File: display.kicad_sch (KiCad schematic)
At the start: 9 parts

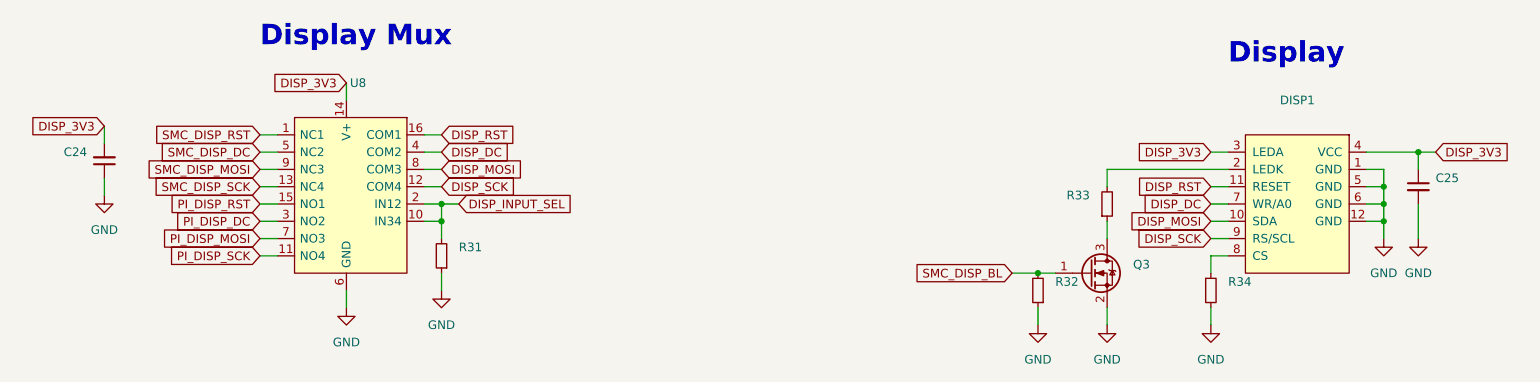
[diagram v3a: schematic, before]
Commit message: layout: update footprint for TP4056M
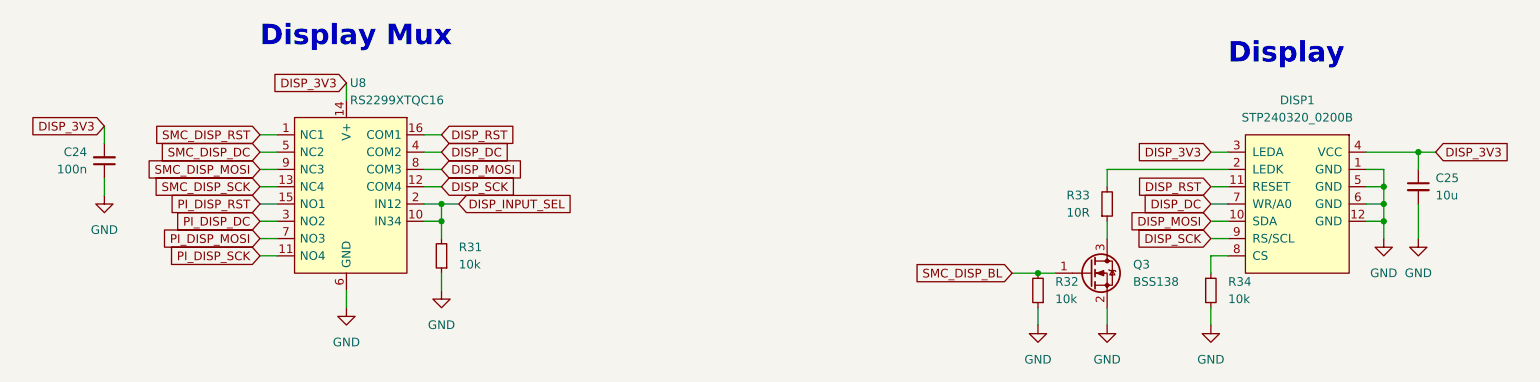
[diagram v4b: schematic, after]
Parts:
- C24: value (none) -> 100n; footprint (none) -> Capacitor_SMD:C_0402_1005Metric
- C25: value (none) -> 10u; footprint (none) -> Capacitor_SMD:C_0402_1005Metric
- DISP1: value (none) -> STP240320_0200B; footprint (none) -> Connector_Molex:Molex_SlimStack_54722-0164_2x08_P0.50mm_Vertical
- Q3: value (none) -> BSS138; footprint (none) -> Package_TO_SOT_SMD:SOT-23
- R31, R32, R34: value (none) -> 10k; footprint (none) -> Resistor_SMD:R_0402_1005Metric
- R33: value (none) -> 10R; footprint (none) -> Resistor_SMD:R_0402_1005Metric
- U8: value (none) -> RS2299XTQC16; footprint (none) -> Package_DFN_QFN:QFN-16-1EP_3x3mm_P0.5mm_EP1.7x1.7mm
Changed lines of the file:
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@@
       (effects (font (size 1.27 1.27)) (justify right))
     )
-    (property "Value" "" (id 1) (at 80.5306 96.52 0)
-      (effects (font (size 1.27 1.27)) (justify right))
-    )
-    (property "Footprint" "" (id 2) (at 97.79 88.9 0)
+    (property "Value" "RS2299XTQC16" (id 1) (at 80.5306 96.52 0)
+      (effects (font (size 1.27 1.27)) (justify right))
+    )
+    (property "Footprint" "Package_DFN_QFN:QFN-16-1EP_3x3mm_P0.5mm_EP1.7x1.7mm" (id 2) (at 97.79 88.9 0)
       (effects (font (size 1.27 1.27)) (justify left) hide)
     )
@@
       (effects (font (size 1.27 1.27)) (justify right))
     )
-    (property "Value" "" (id 1) (at 189.23 113.0299 0)
-      (effects (font (size 1.27 1.27)) (justify right))
-    )
-    (property "Footprint" "" (id 2) (at 191.77 111.76 0)
+    (property "Value" "10R" (id 1) (at 189.23 113.0299 0)
+      (effects (font (size 1.27 1.27)) (justify right))
+    )
+    (property "Footprint" "Resistor_SMD:R_0402_1005Metric" (id 2) (at 191.77 111.76 0)
       (effects (font (size 1.27 1.27)) hide)
     )
@@
       (effects (font (size 1.27 1.27)) (justify right))
     )
-    (property "Value" "" (id 1) (at 96.52 120.6499 0)
-      (effects (font (size 1.27 1.27)) (justify right))
-    )
-    (property "Footprint" "" (id 2) (at 93.98 119.38 0)
+    (property "Value" "10k" (id 1) (at 96.52 120.6499 0)
+      (effects (font (size 1.27 1.27)) (justify right))
+    )
+    (property "Footprint" "Resistor_SMD:R_0402_1005Metric" (id 2) (at 93.98 119.38 0)
       (effects (font (size 1.27 1.27)) hide)
     )
@@
     (in_bom yes) (on_board yes) (fields_autoplaced)
     (property "Reference" "DISP1" (id 0) (at 219.71 96.52 0))
-    (property "Value" "" (id 1) (at 219.71 99.06 0))
-    (property "Footprint" "" (id 2) (at 219.71 101.6 0)
+    (property "Value" "STP240320_0200B" (id 1) (at 219.71 99.06 0))
+    (property "Footprint" "Connector_Molex:Molex_SlimStack_54722-0164_2x08_P0.50mm_Vertical" (id 2) (at 219.71 101.6 0)
       (effects (font (size 1.27 1.27)) hide)
     )
@@
       (effects (font (size 1.27 1.27)) (justify right))
     )
-    (property "Value" "" (id 1) (at 184.15 125.7299 0)
-      (effects (font (size 1.27 1.27)) (justify right))
-    )
-    (property "Footprint" "" (id 2) (at 181.61 124.46 0)
+    (property "Value" "10k" (id 1) (at 184.15 125.7299 0)
+      (effects (font (size 1.27 1.27)) (justify right))
+    )
+    (property "Footprint" "Resistor_SMD:R_0402_1005Metric" (id 2) (at 181.61 124.46 0)
       (effects (font (size 1.27 1.27)) hide)
     )
@@
       (effects (font (size 1.27 1.27)) (justify left))
     )
-    (property "Value" "" (id 1) (at 209.55 125.7299 0)
-      (effects (font (size 1.27 1.27)) (justify left))
-    )
-    (property "Footprint" "" (id 2) (at 207.01 124.46 0)
+    (property "Value" "10k" (id 1) (at 209.55 125.7299 0)
+      (effects (font (size 1.27 1.27)) (justify left))
+    )
+    (property "Footprint" "Resistor_SMD:R_0402_1005Metric" (id 2) (at 207.01 124.46 0)
       (effects (font (size 1.27 1.27)) hide)
     )
@@
       (effects (font (size 1.27 1.27)) (justify left))
     )
-    (property "Value" "" (id 1) (at 240.03 110.4962 0)
-      (effects (font (size 1.27 1.27)) (justify left))
-    )
-    (property "Footprint" "" (id 2) (at 237.49 109.22 0)
+    (property "Value" "10u" (id 1) (at 240.03 110.4962 0)
+      (effects (font (size 1.27 1.27)) (justify left))
+    )
+    (property "Footprint" "Capacitor_SMD:C_0402_1005Metric" (id 2) (at 237.49 109.22 0)
       (effects (font (size 1.27 1.27)) hide)
     )
@@
       (effects (font (size 1.27 1.27)) (justify right))
     )
-    (property "Value" "" (id 1) (at 41.91 106.6735 0)
-      (effects (font (size 1.27 1.27)) (justify right))
-    )
-    (property "Footprint" "" (id 2) (at 44.45 105.41 0)
+    (property "Value" "100n" (id 1) (at 41.91 106.6735 0)
+      (effects (font (size 1.27 1.27)) (justify right))
+    )
+    (property "Footprint" "Capacitor_SMD:C_0402_1005Metric" (id 2) (at 44.45 105.41 0)
       (effects (font (size 1.27 1.27)) hide)
     )
@@
       (effects (font (size 1.27 1.27)) (justify left))
     )
-    (property "Value" "" (id 1) (at 195.58 123.1899 0)
-      (effects (font (size 1.27 1.27)) (justify left))
-    )
-    (property "Footprint" "" (id 2) (at 194.31 123.825 0)
+    (property "Value" "BSS138" (id 1) (at 195.58 123.1899 0)
+      (effects (font (size 1.27 1.27)) (justify left))
+    )
+    (property "Footprint" "Package_TO_SOT_SMD:SOT-23" (id 2) (at 194.31 123.825 0)
       (effects (font (size 1.27 1.27) italic) (justify left) hide)
     )

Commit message: routing: begin routing
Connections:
- net DISP_DC: now also U8.16 (COM1); no longer U8.4 (COM2)
- net DISP_MOSI: now also U8.4 (COM2); no longer U8.8 (COM3)
- net DISP_RST: now also U8.8 (COM3); no longer U8.16 (COM1)
- net PI_DISP_DC: now also U8.15 (NO1); no longer U8.3 (NO2)
- net PI_DISP_MOSI: now also U8.3 (NO2); no longer U8.7 (NO3)
- net PI_DISP_RST: now also U8.7 (NO3); no longer U8.15 (NO1)
- net SMC_DISP_DC: now also U8.1 (NC1); no longer U8.5 (NC2)
- net SMC_DISP_MOSI: now also U8.5 (NC2); no longer U8.9 (NC3)
- net SMC_DISP_RST: now also U8.9 (NC3); no longer U8.1 (NC1)
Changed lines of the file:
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@@
     )
   )
-  (global_label "SMC_DISP_RST" (shape input) (at 67.31 101.6 180) (fields_autoplaced)
+  (global_label "SMC_DISP_RST" (shape input) (at 67.31 106.68 180) (fields_autoplaced)
     (effects (font (size 1.27 1.27)) (justify right))
-    (property "Intersheet References" "${INTERSHEET_REFS}" (id 0) (at 51.2293 101.5206 0)
+    (property "Intersheet References" "${INTERSHEET_REFS}" (id 0) (at 51.2293 106.6006 0)
       (effects (font (size 1.27 1.27)) (justify right) hide)
     )
@@
     )
   )
-  (global_label "PI_DISP_MOSI" (shape input) (at 67.31 116.84 180) (fields_autoplaced)
+  (global_label "PI_DISP_MOSI" (shape input) (at 67.31 114.3 180) (fields_autoplaced)
     (effects (font (size 1.27 1.27)) (justify right))
-    (property "Intersheet References" "${INTERSHEET_REFS}" (id 0) (at 52.1364 116.7606 0)
+    (property "Intersheet References" "${INTERSHEET_REFS}" (id 0) (at 52.1364 114.2206 0)
       (effects (font (size 1.27 1.27)) (justify right) hide)
     )
   )
-  (global_label "DISP_MOSI" (shape input) (at 93.98 106.68 0) (fields_autoplaced)
+  (global_label "DISP_MOSI" (shape input) (at 93.98 104.14 0) (fields_autoplaced)
     (effects (font (size 1.27 1.27)) (justify left))
-    (property "Intersheet References" "${INTERSHEET_REFS}" (id 0) (at 106.3112 106.6006 0)
+    (property "Intersheet References" "${INTERSHEET_REFS}" (id 0) (at 106.3112 104.0606 0)
       (effects (font (size 1.27 1.27)) (justify left) hide)
     )
   )
-  (global_label "DISP_RST" (shape input) (at 93.98 101.6 0) (fields_autoplaced)
+  (global_label "DISP_RST" (shape input) (at 93.98 106.68 0) (fields_autoplaced)
     (effects (font (size 1.27 1.27)) (justify left))
-    (property "Intersheet References" "${INTERSHEET_REFS}" (id 0) (at 105.1621 101.5206 0)
+    (property "Intersheet References" "${INTERSHEET_REFS}" (id 0) (at 105.1621 106.6006 0)
       (effects (font (size 1.27 1.27)) (justify left) hide)
     )
@@
     )
   )
-  (global_label "SMC_DISP_MOSI" (shape input) (at 67.31 106.68 180) (fields_autoplaced)
+  (global_label "SMC_DISP_MOSI" (shape input) (at 67.31 104.14 180) (fields_autoplaced)
     (effects (font (size 1.27 1.27)) (justify right))
-    (property "Intersheet References" "${INTERSHEET_REFS}" (id 0) (at 50.0802 106.7594 0)
+    (property "Intersheet References" "${INTERSHEET_REFS}" (id 0) (at 50.0802 104.2194 0)
       (effects (font (size 1.27 1.27)) (justify right) hide)
     )
@@
     )
   )
-  (global_label "PI_DISP_RST" (shape input) (at 67.31 111.76 180) (fields_autoplaced)
+  (global_label "PI_DISP_RST" (shape input) (at 67.31 116.84 180) (fields_autoplaced)
     (effects (font (size 1.27 1.27)) (justify right))
-    (property "Intersheet References" "${INTERSHEET_REFS}" (id 0) (at 53.2855 111.6806 0)
+    (property "Intersheet References" "${INTERSHEET_REFS}" (id 0) (at 53.2855 116.7606 0)
       (effects (font (size 1.27 1.27)) (justify right) hide)
     )
@@
     )
   )
-  (global_label "DISP_DC" (shape input) (at 93.98 104.14 0) (fields_autoplaced)
+  (global_label "DISP_DC" (shape input) (at 93.98 101.6 0) (fields_autoplaced)
     (effects (font (size 1.27 1.27)) (justify left))
-    (property "Intersheet References" "${INTERSHEET_REFS}" (id 0) (at 104.255 104.0606 0)
+    (property "Intersheet References" "${INTERSHEET_REFS}" (id 0) (at 104.255 101.5206 0)
       (effects (font (size 1.27 1.27)) (justify left) hide)
     )
   )
-  (global_label "SMC_DISP_DC" (shape input) (at 67.31 104.14 180) (fields_autoplaced)
+  (global_label "SMC_DISP_DC" (shape input) (at 67.31 101.6 180) (fields_autoplaced)
     (effects (font (size 1.27 1.27)) (justify right))
-    (property "Intersheet References" "${INTERSHEET_REFS}" (id 0) (at 52.1364 104.0606 0)
+    (property "Intersheet References" "${INTERSHEET_REFS}" (id 0) (at 52.1364 101.5206 0)
       (effects (font (size 1.27 1.27)) (justify right) hide)
     )
@@
     )
   )
-  (global_label "PI_DISP_DC" (shape input) (at 67.31 114.3 180) (fields_autoplaced)
+  (global_label "PI_DISP_DC" (shape input) (at 67.31 111.76 180) (fields_autoplaced)
     (effects (font (size 1.27 1.27)) (justify right))
-    (property "Intersheet References" "${INTERSHEET_REFS}" (id 0) (at 54.1926 114.2206 0)
+    (property "Intersheet References" "${INTERSHEET_REFS}" (id 0) (at 54.1926 111.6806 0)
       (effects (font (size 1.27 1.27)) (justify right) hide)
     )

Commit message: layout, routing: relayout and reroute board
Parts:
- C24: value 100n -> (none); footprint Capacitor_SMD:C_0402_1005Metric -> (none)
- C25: value 10u -> (none); footprint Capacitor_SMD:C_0402_1005Metric -> (none)
- DISP1: value STP240320_0200B -> (none); footprint Connector_Molex:Molex_SlimStack_54722-0164_2x08_P0.50mm_Vertical -> (none)
- Q3: value BSS138 -> (none); footprint Package_TO_SOT_SMD:SOT-23 -> (none)
- R31, R32, R34: value 10k -> (none); footprint Resistor_SMD:R_0402_1005Metric -> (none)
- R33: value 10R -> (none); footprint Resistor_SMD:R_0402_1005Metric -> (none)
- U8: value RS2299XTQC16 -> (none); footprint Package_DFN_QFN:QFN-16-1EP_3x3mm_P0.5mm_EP1.7x1.7mm -> (none)
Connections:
- net DISP_BL_MOS_D: now reaches Q3.3 (D), R33.1
- net DISP_LEDK: now reaches DISP1.2 (LEDK), R33.2
- net DISP_CS: now reaches DISP1.8 (CS), R34.1
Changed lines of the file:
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@@
     (effects (font (size 3 3) (thickness 0.6) bold) (justify left bottom))
   )
+  (label "DISP_BL_MOS_D" (at 191.77 115.57 180)
+    (effects (font (size 0.8 0.8)) (justify right bottom))
+  )
+  (label "DISP_CS" (at 208.28 119.38 180)
+    (effects (font (size 0.8 0.8)) (justify right bottom))
+  )
+  (label "DISP_LEDK" (at 195.58 106.68 180)
+    (effects (font (size 1.27 1.27)) (justify right bottom))
+  )
   (global_label "DISP_MOSI" (shape input) (at 207.01 114.3 180) (fields_autoplaced)
     (effects (font (size 1.27 1.27)) (justify right))
@@
       (effects (font (size 1.27 1.27)) (justify right))
     )
-    (property "Value" "RS2299XTQC16" (id 1) (at 80.5306 96.52 0)
-      (effects (font (size 1.27 1.27)) (justify right))
-    )
-    (property "Footprint" "Package_DFN_QFN:QFN-16-1EP_3x3mm_P0.5mm_EP1.7x1.7mm" (id 2) (at 97.79 88.9 0)
+    (property "Value" "" (id 1) (at 80.5306 96.52 0)
+      (effects (font (size 1.27 1.27)) (justify right))
+    )
+    (property "Footprint" "" (id 2) (at 97.79 88.9 0)
       (effects (font (size 1.27 1.27)) (justify left) hide)
     )
@@
       (effects (font (size 1.27 1.27)) (justify right))
     )
-    (property "Value" "10R" (id 1) (at 189.23 113.0299 0)
-      (effects (font (size 1.27 1.27)) (justify right))
-    )
-    (property "Footprint" "Resistor_SMD:R_0402_1005Metric" (id 2) (at 191.77 111.76 0)
+    (property "Value" "" (id 1) (at 189.23 113.0299 0)
+      (effects (font (size 1.27 1.27)) (justify right))
+    )
+    (property "Footprint" "" (id 2) (at 191.77 111.76 0)
       (effects (font (size 1.27 1.27)) hide)
     )
@@
       (effects (font (size 1.27 1.27)) (justify right))
     )
-    (property "Value" "10k" (id 1) (at 96.52 120.6499 0)
-      (effects (font (size 1.27 1.27)) (justify right))
-    )
-    (property "Footprint" "Resistor_SMD:R_0402_1005Metric" (id 2) (at 93.98 119.38 0)
+    (property "Value" "" (id 1) (at 96.52 120.6499 0)
+      (effects (font (size 1.27 1.27)) (justify right))
+    )
+    (property "Footprint" "" (id 2) (at 93.98 119.38 0)
       (effects (font (size 1.27 1.27)) hide)
     )
@@
     (in_bom yes) (on_board yes) (fields_autoplaced)
     (property "Reference" "DISP1" (id 0) (at 219.71 96.52 0))
-    (property "Value" "STP240320_0200B" (id 1) (at 219.71 99.06 0))
-    (property "Footprint" "Connector_Molex:Molex_SlimStack_54722-0164_2x08_P0.50mm_Vertical" (id 2) (at 219.71 101.6 0)
+    (property "Value" "" (id 1) (at 219.71 99.06 0))
+    (property "Footprint" "" (id 2) (at 219.71 101.6 0)
       (effects (font (size 1.27 1.27)) hide)
     )
@@
       (effects (font (size 1.27 1.27)) (justify right))
     )
-    (property "Value" "10k" (id 1) (at 184.15 125.7299 0)
-      (effects (font (size 1.27 1.27)) (justify right))
-    )
-    (property "Footprint" "Resistor_SMD:R_0402_1005Metric" (id 2) (at 181.61 124.46 0)
+    (property "Value" "" (id 1) (at 184.15 125.7299 0)
+      (effects (font (size 1.27 1.27)) (justify right))
+    )
+    (property "Footprint" "" (id 2) (at 181.61 124.46 0)
       (effects (font (size 1.27 1.27)) hide)
     )
@@
       (effects (font (size 1.27 1.27)) (justify left))
     )
-    (property "Value" "10k" (id 1) (at 209.55 125.7299 0)
-      (effects (font (size 1.27 1.27)) (justify left))
-    )
-    (property "Footprint" "Resistor_SMD:R_0402_1005Metric" (id 2) (at 207.01 124.46 0)
+    (property "Value" "" (id 1) (at 209.55 125.7299 0)
+      (effects (font (size 1.27 1.27)) (justify left))
+    )
+    (property "Footprint" "" (id 2) (at 207.01 124.46 0)
       (effects (font (size 1.27 1.27)) hide)
     )
@@
       (effects (font (size 1.27 1.27)) (justify left))
     )
-    (property "Value" "10u" (id 1) (at 240.03 110.4962 0)
-      (effects (font (size 1.27 1.27)) (justify left))
-    )
-    (property "Footprint" "Capacitor_SMD:C_0402_1005Metric" (id 2) (at 237.49 109.22 0)
+    (property "Value" "" (id 1) (at 240.03 110.4962 0)
+      (effects (font (size 1.27 1.27)) (justify left))
+    )
+    (property "Footprint" "" (id 2) (at 237.49 109.22 0)
       (effects (font (size 1.27 1.27)) hide)
     )
@@
       (effects (font (size 1.27 1.27)) (justify right))
     )
-    (property "Value" "100n" (id 1) (at 41.91 106.6735 0)
-      (effects (font (size 1.27 1.27)) (justify right))
-    )
-    (property "Footprint" "Capacitor_SMD:C_0402_1005Metric" (id 2) (at 44.45 105.41 0)
+    (property "Value" "" (id 1) (at 41.91 106.6735 0)
+      (effects (font (size 1.27 1.27)) (justify right))
+    )
+    (property "Footprint" "" (id 2) (at 44.45 105.41 0)
       (effects (font (size 1.27 1.27)) hide)
     )
@@
       (effects (font (size 1.27 1.27)) (justify left))
     )
-    (property "Value" "BSS138" (id 1) (at 195.58 123.1899 0)
-      (effects (font (size 1.27 1.27)) (justify left))
-    )
-    (property "Footprint" "Package_TO_SOT_SMD:SOT-23" (id 2) (at 194.31 123.825 0)
+    (property "Value" "" (id 1) (at 195.58 123.1899 0)
+      (effects (font (size 1.27 1.27)) (justify left))
+    )
+    (property "Footprint" "" (id 2) (at 194.31 123.825 0)
       (effects (font (size 1.27 1.27) italic) (justify left) hide)
     )

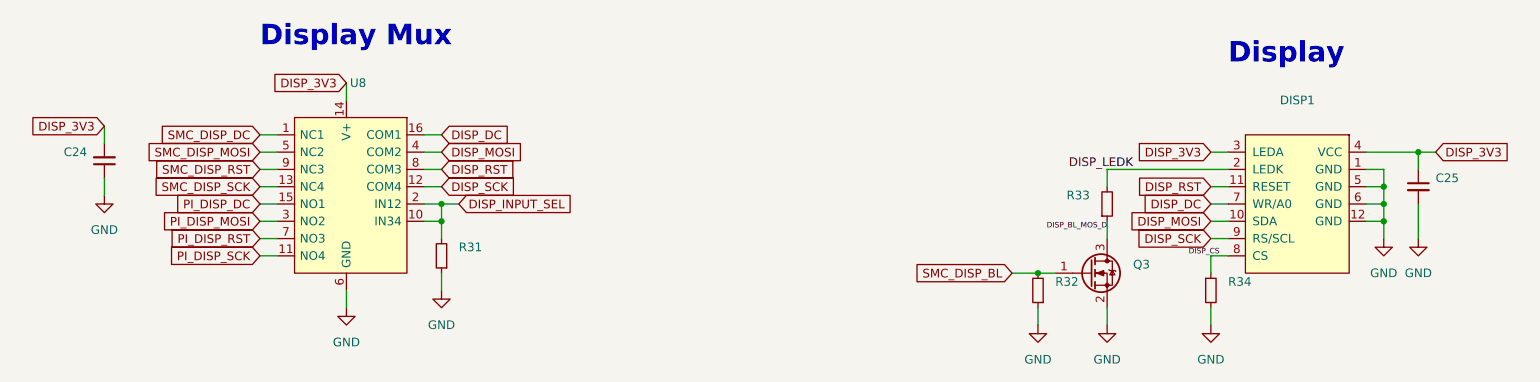
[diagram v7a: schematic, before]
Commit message: layout: add testpoints, extra mounting hole, grounding clips
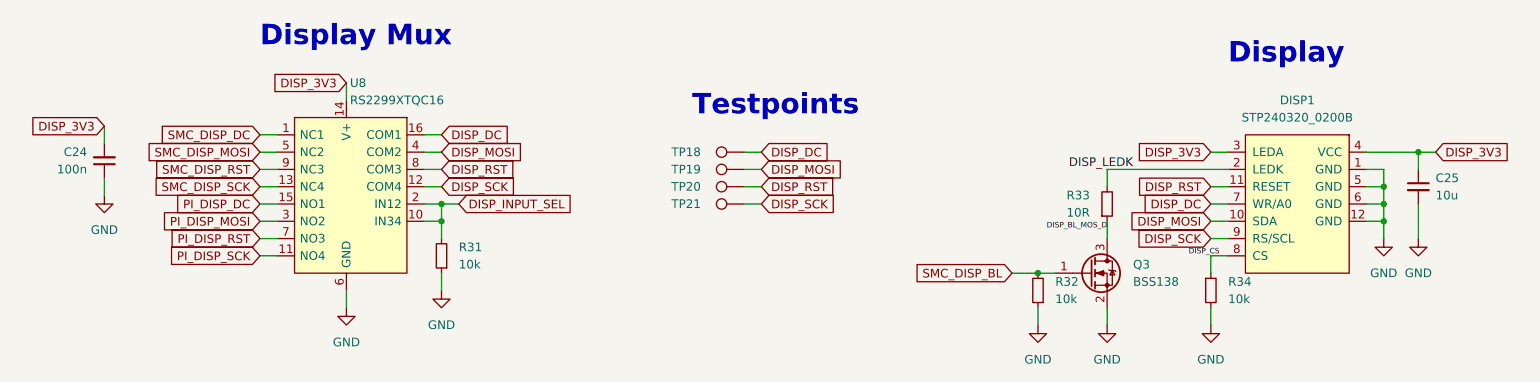
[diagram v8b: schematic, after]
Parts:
- added TP18, TP19, TP20, TP21: TestPoint, TestPoint:TestPoint_Pad_D1.5mm, symbol Connector:TestPoint
- C24: value (none) -> 100n; footprint (none) -> Capacitor_SMD:C_0402_1005Metric
- C25: value (none) -> 10u; footprint (none) -> Capacitor_SMD:C_0402_1005Metric
- DISP1: value (none) -> STP240320_0200B; footprint (none) -> Connector_Molex:Molex_SlimStack_54722-0164_2x08_P0.50mm_Vertical
- Q3: value (none) -> BSS138; footprint (none) -> Package_TO_SOT_SMD:SOT-23
- R31, R32, R34: value (none) -> 10k; footprint (none) -> Resistor_SMD:R_0402_1005Metric
- R33: value (none) -> 10R; footprint (none) -> Resistor_SMD:R_0402_1005Metric
- U8: value (none) -> RS2299XTQC16; footprint (none) -> Package_DFN_QFN:QFN-16-1EP_3x3mm_P0.5mm_EP1.7x1.7mm
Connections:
- net DISP_DC: now also TP18.1
- net DISP_MOSI: now also TP19.1
- net DISP_RST: now also TP20.1
- net DISP_SCK: now also TP21.1
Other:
- note added: "Testpoints"
